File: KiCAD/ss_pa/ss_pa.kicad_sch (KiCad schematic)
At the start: 0 parts

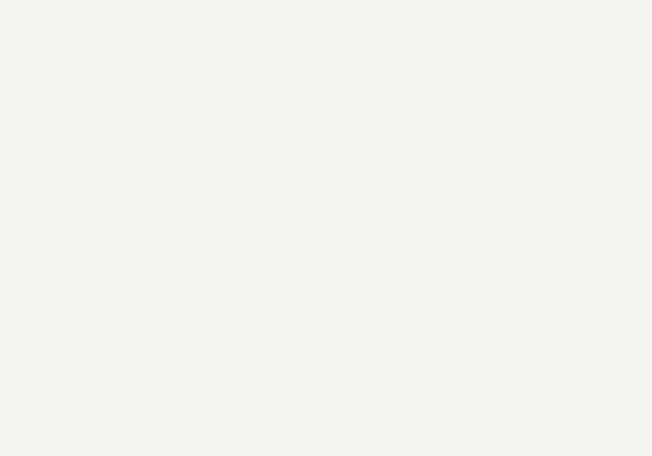
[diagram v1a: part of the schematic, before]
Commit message: KiCad revC: ss_pa add Fault_Shutdown hierarchical sheet skeleton
New empty sub-sheet (fault_shutdown.kicad_sch) + reference added to
ss_pa root. Will hold the hardware overcurrent latch (LM393 with
self-latching positive feedback, 2x 2N7000 shunting Bias_A/B to GND
on fault, reset pushbutton, FAULT LED, FAULT net exported to Metro
GPIO). Design spec documented in chat; user to populate the sheet
with KiCad standard-library symbols (Comparator:LM393,
Transistor_FET:2N7000, Device:R/LED/C, Switch:SW_Push) per that spec.

Co-Authored-By: Claude Opus 4.7 <noreply@anthropic.com>
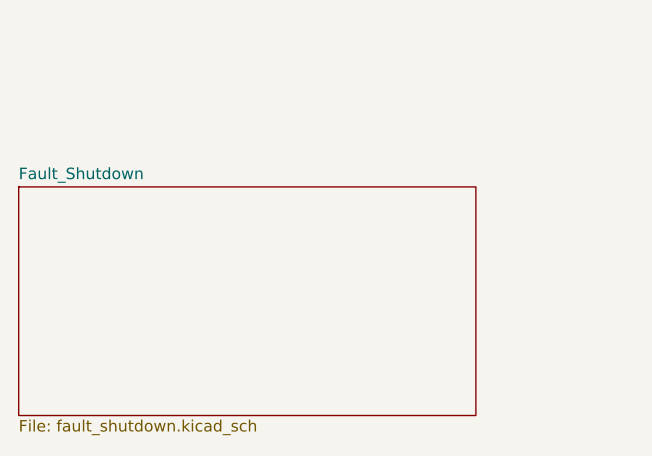
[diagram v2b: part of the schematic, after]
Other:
- added sheet Fault_Shutdown (fault_shutdown.kicad_sch)
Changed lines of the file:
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@@
+		)
+	)
+	(sheet
+		(at 50.8 100.33)
+		(size 50.8 25.4)
+		(exclude_from_sim no)
+		(in_bom yes)
+		(on_board yes)
+		(dnp no)
+		(fields_autoplaced yes)
+		(stroke
+			(width 0.1524)
+			(type solid)
+		)
+		(fill
+			(color 0 0 0 0)
+		)
+		(property "Sheetname" "Fault_Shutdown"
+			(at 50.8 99.6184 0)
+			(show_name no)
+			(do_not_autoplace no)
+			(effects
+				(font
+					(size 1.27 1.27)
+				)
+				(justify left bottom)
+			)
+		)
+		(property "Sheetfile" "fault_shutdown.kicad_sch"
+			(at 50.8 126.1746 0)
+			(show_name no)
+			(do_not_autoplace no)
+			(effects
+				(font
+					(size 1.27 1.27)
+				)
+				(justify left top)
+			)
+		)
+		(instances
+			(project "ss_pa"
+				(path "/7b9fe991-54d6-43c4-a637-0ed9ee982c42"
+					(page "4")
+				)
+			)
 		)
 	)

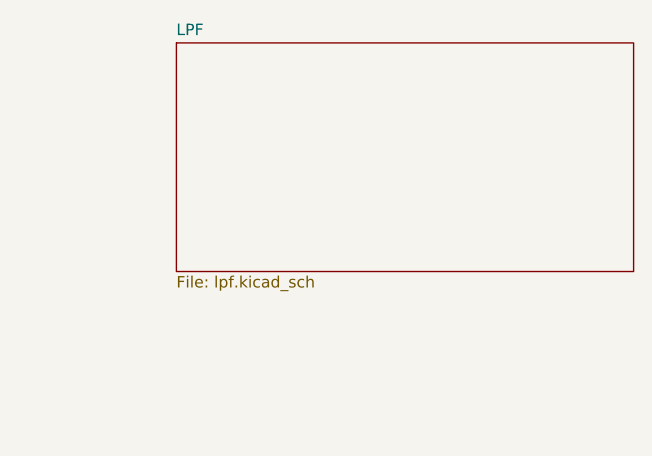
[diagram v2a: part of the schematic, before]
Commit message: revD: drop stale LPF sub-sheets from analog + ss_pa, scrub 13.8V text comments
- Remove hierarchical LPF sub-sheets from analog and ss_pa roots; LPF
  now lives in its own project (KiCAD/Output LPF/).
- Delete the skeleton lpf.kicad_sch files and corresponding entries
  from both .kicad_pro sheet-UUID lists.
- Scrub two stale text annotations on analog/power.kicad_sch:
  "13.8V in" -> "Shack supply in" and the J5/J33/J34 legend box.
  13.8V now only appears on ss_pa and the shared +13.8V power-symbol
  definition in xmitter.kicad_sym.

Co-Authored-By: Claude Opus 4.7 <noreply@anthropic.com>
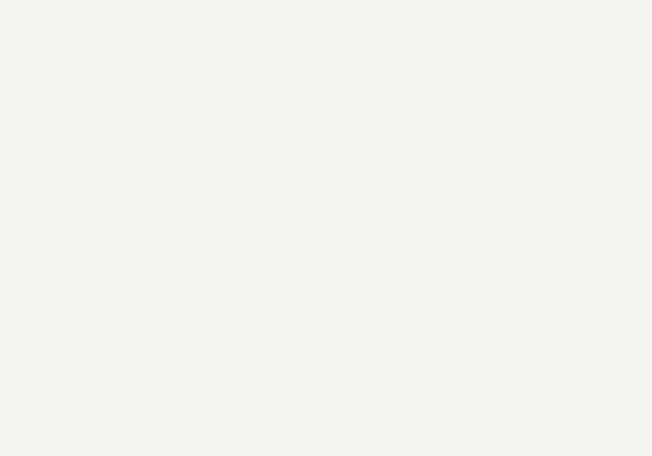
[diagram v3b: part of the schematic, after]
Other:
- removed sheet LPF
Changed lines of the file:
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@@
 	(paper "A4")
-	(sheet
-		(at 127 50.8)
-		(size 50.8 25.4)
-		(exclude_from_sim no)
-		(in_bom yes)
-		(on_board yes)
-		(dnp no)
-		(fields_autoplaced yes)
-		(stroke
-			(width 0.1524)
-			(type solid)
-		)
-		(fill
-			(color 0 0 0 0)
-		)
-		(property "Sheetname" "LPF"
-			(at 127 50.0884 0)
-			(show_name no)
-			(do_not_autoplace no)
-			(effects
-				(font
-					(size 1.27 1.27)
-				)
-				(justify left bottom)
-			)
-		)
-		(property "Sheetfile" "lpf.kicad_sch"
-			(at 127 76.6446 0)
-			(show_name no)
-			(do_not_autoplace no)
-			(effects
-				(font
-					(size 1.27 1.27)
-				)
-				(justify left top)
-			)
-		)
-		(instances
-			(project "ss_pa"
-				(path "/7b9fe991-54d6-43c4-a637-0ed9ee982c42"
-					(page "3")
-				)
-			)
-		)
-	)
 	(sheet
 		(at 50.8 50.8)

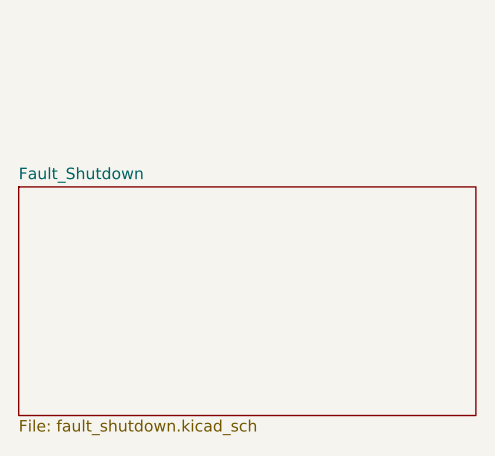
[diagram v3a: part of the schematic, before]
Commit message: revD: U18 heartbeat RC reset + fault_shutdown migrated to analog
- arduino.kicad_sch: R48 10K + C14 10uF RC on U18 RST_A holds
  CD14538B heartbeat watchdog in reset ~70-120ms during Metro boot,
  preventing SS_PWR_RLY / SS_PA_INRUSH false-energize while PCF8575
  defaults HIGH on its outputs
- fault_shutdown.kicad_sch (new): LM393 overcurrent trip +
  CD74HC4066 bias switch + V_REF latch migrated from ss_pa to
  analog so FAULT_N stays off the umbilical; co-located with the
  Metro that reads it. Ref numbers +200 to avoid collision with
  pre-existing analog refs
- analog.kicad_sch: adds Fault_Shutdown sub-sheet reference (page 11)
- ss_pa: fault_shutdown sheet reference removed; ss_pa.net reflects
  the component loss (eliminates ss_pa U3 LM2936 LDO and +5V rail
  dependency)
- pa_stage.kicad_sch: R1-R4 bumped to 2W (RSF200JT-73-0R22) with
  DIN0516 L15.5mm footprint; footprint cleanup pass
- power.kicad_sch: 4.7R dummy bumped to 4.7R 10W with Axial_Power
  L25.0mm W9.0mm P30.48mm footprint

Co-Authored-By: Claude Opus 4.7 <noreply@anthropic.com>
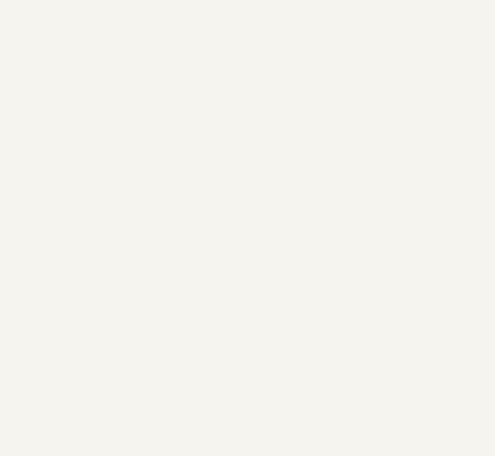
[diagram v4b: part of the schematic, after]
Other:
- removed sheet Fault_Shutdown
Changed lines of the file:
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@@
-		)
-	)
-	(sheet
-		(at 50.8 100.33)
-		(size 50.8 25.4)
-		(exclude_from_sim no)
-		(in_bom yes)
-		(on_board yes)
-		(dnp no)
-		(fields_autoplaced yes)
-		(stroke
-			(width 0.1524)
-			(type solid)
-		)
-		(fill
-			(color 0 0 0 0)
-		)
-		(property "Sheetname" "Fault_Shutdown"
-			(at 50.8 99.6184 0)
-			(show_name no)
-			(do_not_autoplace no)
-			(effects
-				(font
-					(size 1.27 1.27)
-				)
-				(justify left bottom)
-			)
-		)
-		(property "Sheetfile" "fault_shutdown.kicad_sch"
-			(at 50.8 126.1746 0)
-			(show_name no)
-			(do_not_autoplace no)
-			(effects
-				(font
-					(size 1.27 1.27)
-				)
-				(justify left top)
-			)
-		)
-		(instances
-			(project "ss_pa"
-				(path "/7b9fe991-54d6-43c4-a637-0ed9ee982c42"
-					(page "4")
-				)
-			)
 		)
 	)
